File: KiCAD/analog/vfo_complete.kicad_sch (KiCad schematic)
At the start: 114 parts, among them J1 Filter Out, J10 Filter Out, J2 Filter Out, J3 Conn_01x02_Pin, J5 Conn_01x02_Pin, Q2 40673, Q3 2N3904, Q8 2N3904, U10 LM7171xIN, U11 LM7171xIN, U12 LM7171xIN, U13 LM7812_TO220, U14 LM317L_TO92, U21 LT1054, U22 LM7805_TO220, U5 Si5351A_Breakout, U9 MCP4921

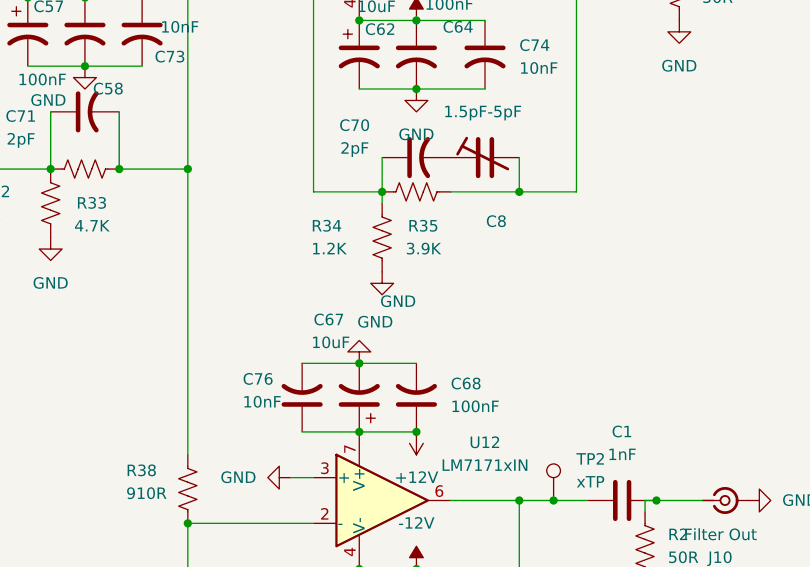
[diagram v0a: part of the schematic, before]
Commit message: KiCad revB: BFC2808 trimmer footprint for C8, verification checklist entry
- New custom footprint: xmitter:Trimmer_Vishay_BFC2808_D5mm_P5.08mm
  (radial THT, 5.08 mm pitch, 1.3 mm drill, Ø 2.4 mm pads, Ø 5.5 mm
  silk housing outline). Targets the top-adjustment 20508 variant of
  the 1.5-5 pF BFC2 808 series.
- Assigned that footprint to C8 (phase-trim cap across R35 in U11
  non-inv feedback). Datasheet property now points at the local PDF.
- Renamed source PDF: bfc2808-5mm.pdf → vishay-trimmer-cap.pdf (from
  a separate git-mv earlier in the session; references updated in
  three places to match).
- pcb_fab_checklist.md: new Section 1 sub-entry for the BFC2808
  footprint flagging (a) the 5.08 mm pitch assumption, (b) required
  1:1 paper-check against the physical part, (c) ordering-variant
  gotcha (20508 vs 23508 have different pitches).
- analog.kicad_pro: KiCad-driven used_designators expansion (RV1,
  #PWR14 added — cosmetic project metadata).

Co-Authored-By: Claude Opus 4.7 <noreply@anthropic.com>
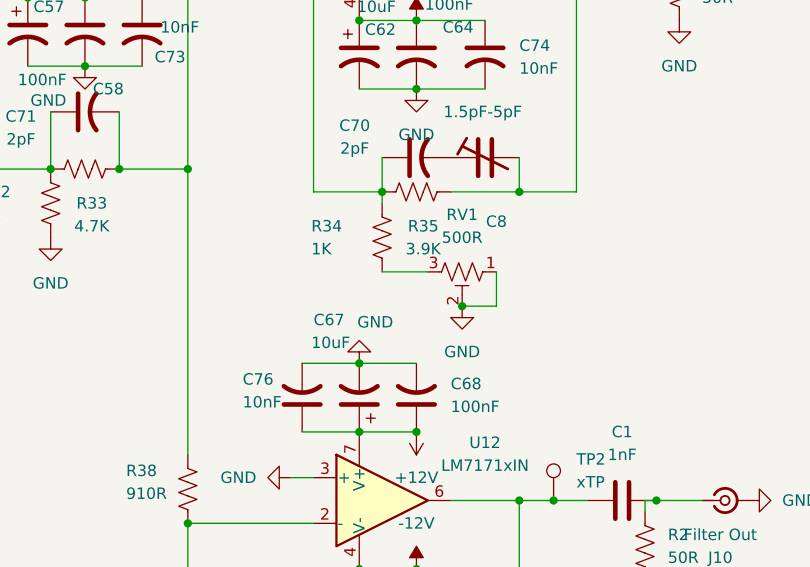
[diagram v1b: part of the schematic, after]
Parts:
- added RV1: 500R, symbol Device:R_Potentiometer_Trim_US
- C8: footprint (none) -> xmitter:Trimmer_Vishay_BFC2808_D5mm_P5.08mm
- R34: value 1.2K -> 1K
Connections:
- net GND: now also RV1.1, RV1.2; no longer R34.2
- new net: R34.2, RV1.3
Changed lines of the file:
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@@
 	)
 	(junction
+		(at 205.74 118.11)
+		(diameter 0)
+		(color 0 0 0 0)
+	)
+	(junction
 		(at 200.66 132.08)
 		(diameter 0)
@@
 	(wire
 		(pts
+			(xy 209.55 118.11) (xy 205.74 118.11)
+		)
+		(stroke
+			(width 0)
+			(type default)
+		)
+	)
+	(wire
+		(pts
 			(xy 147.32 35.56) (xy 149.86 35.56)
 		)
@@
 	(wire
 		(pts
+			(xy 209.55 114.3) (xy 209.55 118.11)
+		)
+		(stroke
+			(width 0)
+			(type default)
+		)
+	)
+	(wire
+		(pts
 			(xy 68.58 184.15) (xy 73.66 184.15)
 		)
@@
 	(wire
 		(pts
+			(xy 196.85 114.3) (xy 201.93 114.3)
+		)
+		(stroke
+			(width 0)
+			(type default)
+		)
+	)
+	(wire
+		(pts
 			(xy 54.61 177.8) (xy 73.66 177.8)
 		)
@@
 	(symbol
 		(lib_id "power:GND")
+		(at 205.74 118.11 0)
+		(unit 1)
+		(body_style 1)
+		(exclude_from_sim no)
+		(in_bom yes)
+		(on_board yes)
+		(in_pos_files yes)
+		(dnp no)
+		(fields_autoplaced yes)
+		(property "Reference" "#PWR014"
+			(at 205.74 124.46 0)
+			(hide yes)
+			(show_name no)
+			(do_not_autoplace no)
+			(effects
+				(font
+					(size 1.27 1.27)
+				)
+			)
+		)
+		(property "Value" "GND"
+			(at 205.74 123.19 0)
+			(show_name no)
+			(do_not_autoplace no)
+			(effects
+				(font
+					(size 1.27 1.27)
+				)
+			)
+		)
+		(property "Footprint" ""
+			(at 205.74 118.11 0)
+			(hide yes)
+			(show_name no)
+			(do_not_autoplace no)
+			(effects
+				(font
+					(size 1.27 1.27)
+				)
+			)
+		)
+		(property "Datasheet" ""
+			(at 205.74 118.11 0)
+			(hide yes)
+			(show_name no)
+			(do_not_autoplace no)
+			(effects
+				(font
+					(size 1.27 1.27)
+				)
+			)
+		)
+		(property "Description" "Power symbol creates a global label with name \"GND\" , ground"
+			(at 205.74 118.11 0)
+			(hide yes)
+			(show_name no)
+			(do_not_autoplace no)
+			(effects
+				(font
+					(size 1.27 1.27)
+				)
+			)
+		)
+		(pin "1"
+		)
+		(instances
+			(project "analog"
+				(path "/d3de40b8-856b-4fbd-829c-f45ffcd55742/94bbc356-fa50-4d6f-b6f0-2ea7eca96dd3"
+					(reference "#PWR014")
+					(unit 1)
+				)
+			)
+		)
+	)
+	(symbol
+		(lib_id "power:GND")
 		(at 43.18 82.55 0)
 		(unit 1)
@@
 			)
 		)
-		(property "Footprint" ""
+		(property "Footprint" "xmitter:Trimmer_Vishay_BFC2808_D5mm_P5.08mm"
 			(at 208.28 101.6 0)
 			(hide yes)
@@
 			)
 		)
-		(property "Datasheet" ""
+		(property "Datasheet" "Documentation/Components/vishay-trimmer-cap.pdf"
 			(at 208.28 101.6 0)
 			(hide yes)
@@
 	)
 	(symbol
+		(lib_id "Device:R_Potentiometer_Trim_US")
+		(at 205.74 114.3 270)
+		(unit 1)
+		(body_style 1)
+		(exclude_from_sim no)
+		(in_bom yes)
+		(on_board yes)
+		(in_pos_files yes)
+		(dnp no)
+		(fields_autoplaced yes)
+		(property "Reference" "RV1"
+			(at 205.74 107.95 90)
+			(show_name no)
+			(do_not_autoplace no)
+			(effects
+				(font
+					(size 1.27 1.27)
+				)
+			)
+		)
+		(property "Value" "500R"
+			(at 205.74 110.49 90)
+			(show_name no)
+			(do_not_autoplace no)
+			(effects
+				(font
+					(size 1.27 1.27)
+				)
+			)
+		)
+		(property "Footprint" ""
+			(at 205.74 114.3 0)
+			(hide yes)
+			(show_name no)
+			(do_not_autoplace no)
+			(effects
+				(font
+					(size 1.27 1.27)
+				)
+			)
+		)
+		(property "Datasheet" ""
+			(at 205.74 114.3 0)
+			(hide yes)
+			(show_name no)
+			(do_not_autoplace no)
+			(effects
+				(font
+					(size 1.27 1.27)
+				)
+			)
+		)
+		(property "Description" "Trim-potentiometer, US symbol"
+			(at 205.74 114.3 0)
+			(hide yes)
+			(show_name no)
+			(do_not_autoplace no)
+			(effects
+				(font
+					(size 1.27 1.27)
+				)
+			)
+		)
+		(property "Sim.Device" "R"
+			(at 205.74 114.3 0)
+			(hide yes)
+			(show_name no)
+			(do_not_autoplace no)
+			(effects
+				(font
+					(size 1.27 1.27)
+				)
+			)
+		)
+		(property "Sim.Type" "POT"
+			(at 205.74 114.3 0)
+			(hide yes)
+			(show_name no)
+			(do_not_autoplace no)
+			(effects
+				(font
+					(size 1.27 1.27)
+				)
+			)
+		)
+		(property "Sim.Pins" "1=r0 2=wiper 3=r1"
+			(at 205.74 114.3 0)
+			(hide yes)
+			(show_name no)
+			(do_not_autoplace no)
+			(effects
+				(font
+					(size 1.27 1.27)
+				)
+			)
+		)
+		(pin "1"
+		)
+		(pin "2"
+		)
+		(pin "3"
+		)
+		(instances
+			(project "analog"
+				(path "/d3de40b8-856b-4fbd-829c-f45ffcd55742/94bbc356-fa50-4d6f-b6f0-2ea7eca96dd3"
+					(reference "RV1")
+					(unit 1)
+				)
+			)
+		)
+	)
+	(symbol
 		(lib_id "power:GND")
 		(at 200.66 154.94 0)
@@
 	(symbol
 		(lib_id "power:GND")
-		(at 196.85 114.3 0)
-		(unit 1)
-		(body_style 1)
-		(exclude_from_sim no)
-		(in_bom yes)
-		(on_board yes)
-		(in_pos_files yes)
-		(dnp no)
-		(property "Reference" "#PWR0144"
-			(at 196.85 120.65 0)
-			(hide yes)
-			(show_name no)
-			(do_not_autoplace no)
-			(effects
-				(font
-					(size 1.27 1.27)
-				)
-			)
-		)
-		(property "Value" "GND"
-			(at 198.628 117.602 0)
-			(show_name no)
-			(do_not_autoplace no)
-			(effects
-				(font
-					(size 1.27 1.27)
-				)
-			)
-		)
-		(property "Footprint" ""
-			(at 196.85 114.3 0)
-			(hide yes)
-			(show_name no)
-			(do_not_autoplace no)
-			(effects
-				(font
-					(size 1.27 1.27)
-				)
-			)
-		)
-		(property "Datasheet" ""
-			(at 196.85 114.3 0)
-			(hide yes)
-			(show_name no)
-			(do_not_autoplace no)
-			(effects
-				(font
-					(size 1.27 1.27)
-				)
-			)
-		)
-		(property "Description" "Power symbol creates a global label with name \"GND\" , ground"
-			(at 196.85 114.3 0)
-			(hide yes)
-			(show_name no)
-			(do_not_autoplace no)
-			(effects
-				(font
-					(size 1.27 1.27)
-				)
-			)
-		)
-		(pin "1"
-		)
-		(instances
-			(project "analog"
-				(path "/d3de40b8-856b-4fbd-829c-f45ffcd55742/94bbc356-fa50-4d6f-b6f0-2ea7eca96dd3"
-					(reference "#PWR0144")
-					(unit 1)
-				)
-			)
-		)
-	)
-	(symbol
-		(lib_id "power:GND")
 		(at 120.65 81.28 0)
 		(unit 1)
@@
 			)
 		)
-		(property "Value" "1.2K"
+		(property "Value" "1K"
 			(at 188.976 111.76 0)
 			(show_name no)

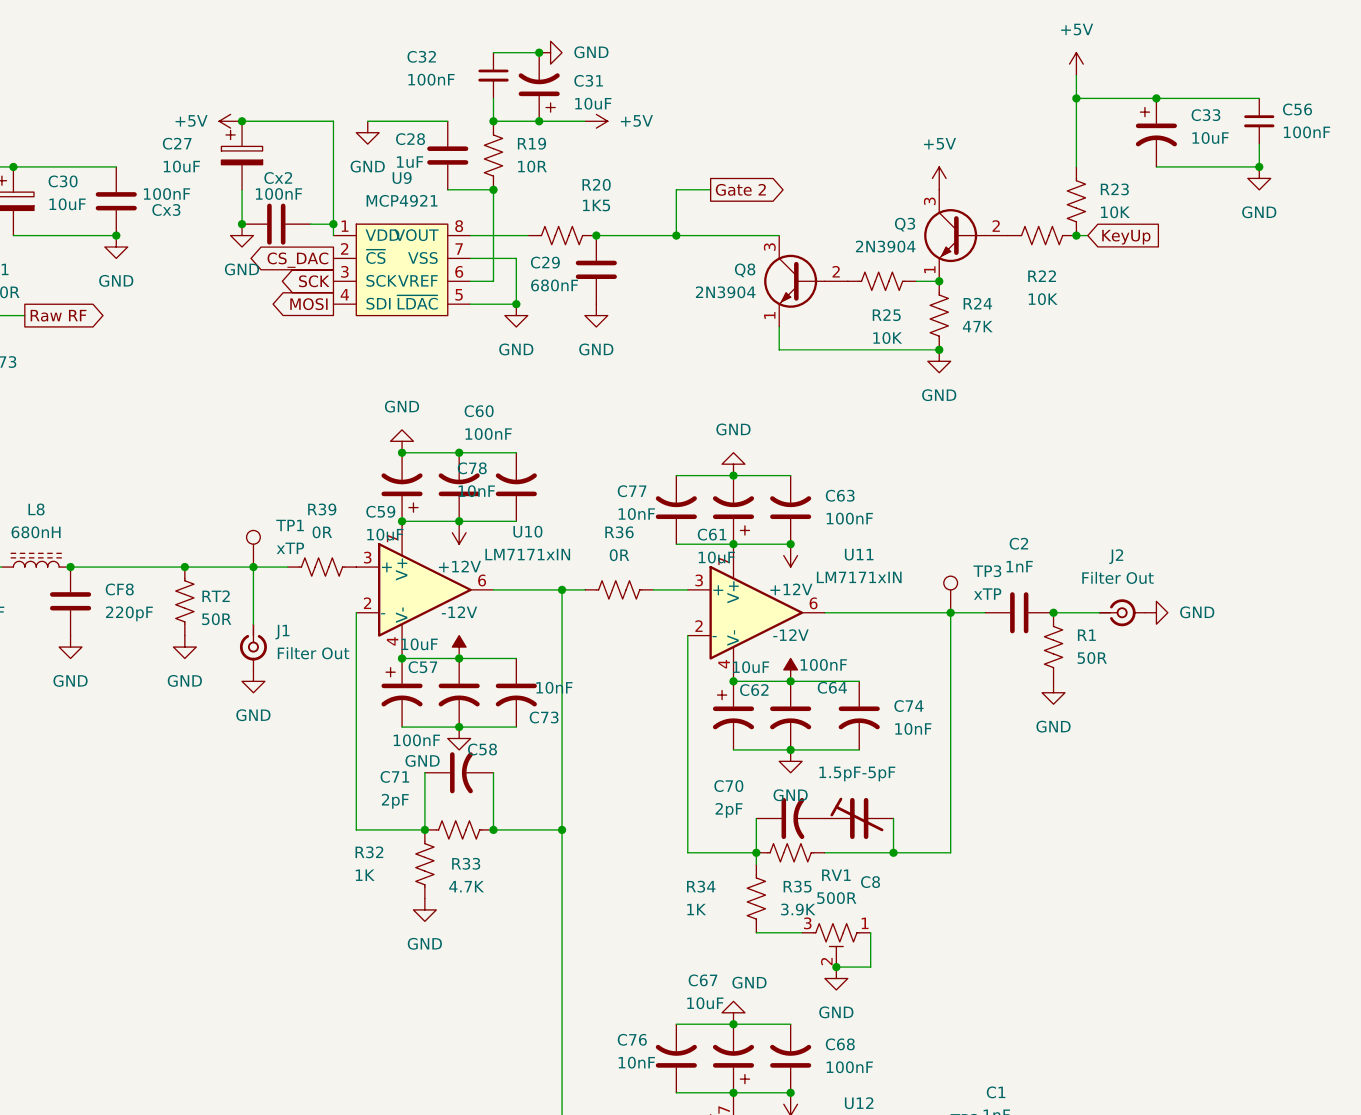
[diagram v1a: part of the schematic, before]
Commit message: revB frozen state: MCP4922 swap + LDAC decouple + sheet rename + protoshield work
Captures the in-flight state of revB at the point where the project pivoted
to a full-SS output stage on a new branch (SS_Rev_C, cut from this commit).
revB is retained as a fallback if the SS PA plan on revC proves inadequate.

Included changes:
- Analog: MCP4921 (single DAC) replaced with MCP4922 (dual DAC). Channel
  assignment: DAC_A -> PA_OUTPUT_LEVEL (new global label, awaiting PA
  board), DAC_B -> Gate 2 (DGFET envelope keyer). Channels swapped from
  initial-design intent for layout convenience.
- Analog: DAC_LDAC_N decoupled from PCF8575 P5 (that global label renamed
  to PCF_P5_SPARE). Intent: route LDAC to Metro A4 for zero-latency
  simultaneous-DAC-update capability. Physical route to A4 NOT yet added
  -- DAC_LDAC_N label on dac.kicad_sch is dangling and will fail ERC.
- Analog: KiCad-driven used_designators bookkeeping (analog.kicad_pro).
- Sheet rename: KiCAD/analog/untitled.kicad_sch -> dac.kicad_sch. Root
  schematic Sheetfile reference updated.
- Protoshield: 537 lines of additions to protoshield.kicad_sch (user
  work). Not reviewed in this commit -- carried forward as-is.
- .gitignore: added tools/_*.py exclusion (local review-helper scripts).

**revB is NOT fab-ready in this state.** See memory
project_revB_pre_fab_check.md (outside repo) for the punch list. If the
SS PA plan ever reverses and someone revives revB, ALL open items must
be closed and a full pass through Documentation/pcb_fab_checklist.md
must be completed before any gerber submit.

Co-Authored-By: Claude Opus 4.7 <noreply@anthropic.com>
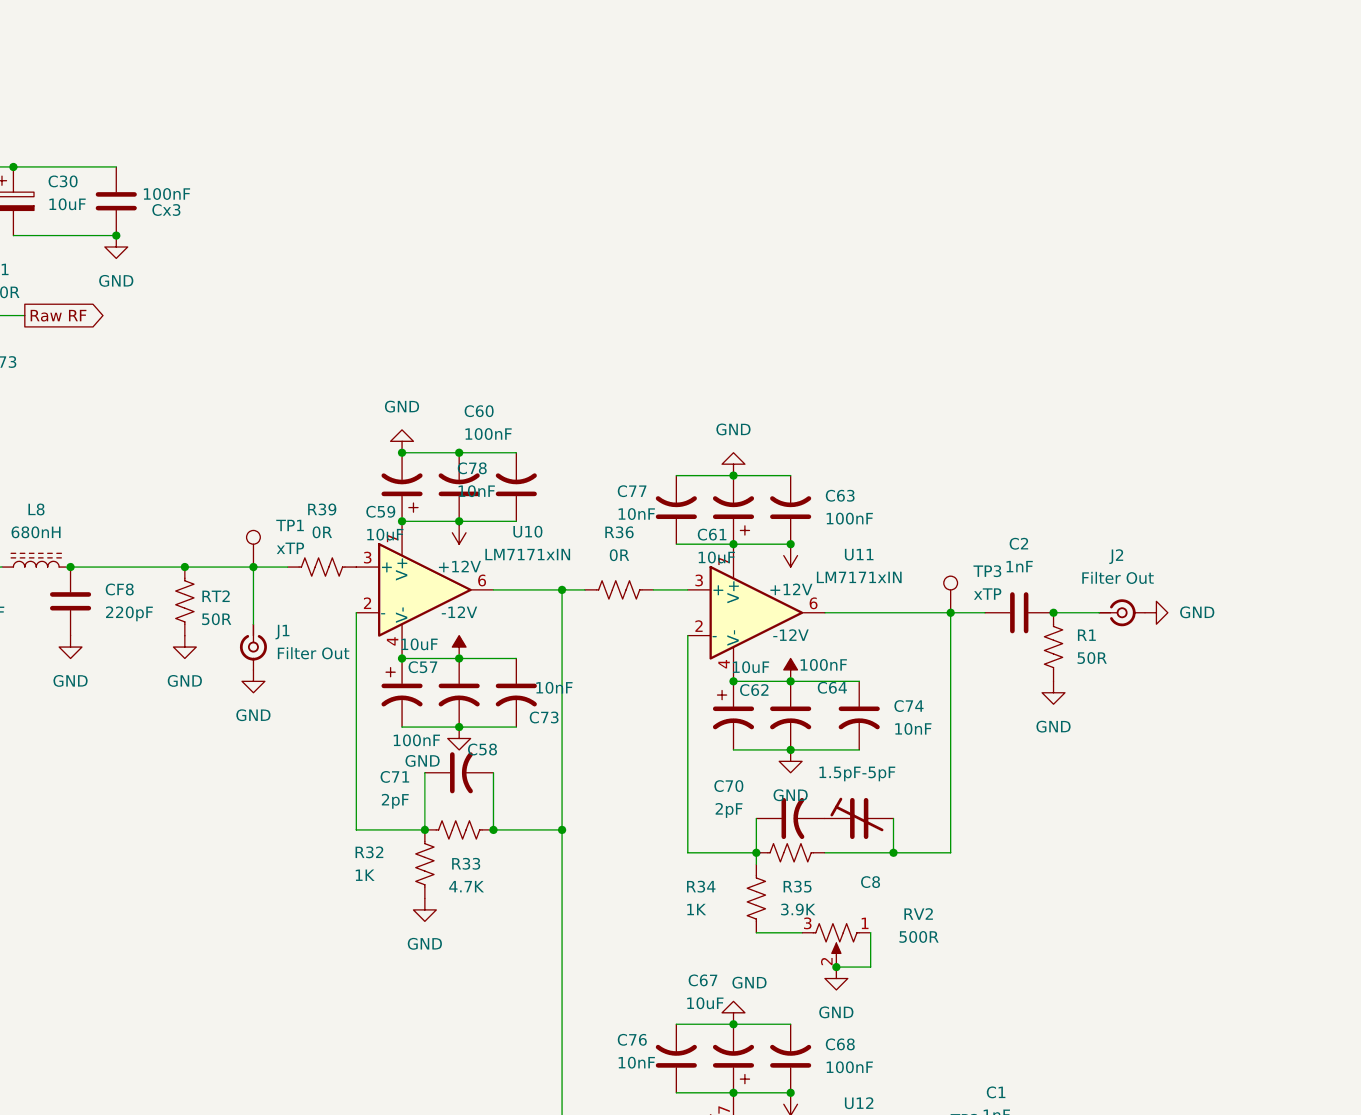
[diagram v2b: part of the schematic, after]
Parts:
- removed C27: 10uF, Capacitor_THT:C_Rect_L7.2mm_W4.5mm_P5.00mm, symbol Device:C_Polarized
- removed C28: 1uF, Capacitor_THT:C_Rect_L7.2mm_W4.5mm_P5.00mm, symbol Device:C
- removed C29: 680nF, Capacitor_THT:C_Rect_L13.0mm_W6.0mm_P10.00mm_FKS3_FKP3_MKS4, symbol Device:C
- removed C31, C33: 10uF, Capacitor_THT:CP_Radial_D5.0mm_P2.00mm, symbol Device:C_Polarized_US
- removed C32, C56: 100nF, Capacitor_THT:C_Disc_D5.0mm_W2.5mm_P5.00mm, symbol Device:C_Small
- removed Cx2: 100nF, Capacitor_THT:C_Disc_D5.0mm_W2.5mm_P5.00mm, symbol Device:C
- removed Q3, Q8: 2N3904, Package_TO_SOT_THT:TO-92_Inline_Wide, symbol Transistor_BJT:2N3904
- removed R19: 10R, Resistor_THT:R_Axial_DIN0207_L6.3mm_D2.5mm_P10.16mm_Horizontal, symbol Device:R_US
- removed R20: 1K5, Resistor_THT:R_Axial_DIN0207_L6.3mm_D2.5mm_P10.16mm_Horizontal, symbol Device:R_US
- removed R22, R23, R25: 10K, Resistor_THT:R_Axial_DIN0207_L6.3mm_D2.5mm_P10.16mm_Horizontal, symbol Device:R_US
- removed R24: 47K, Resistor_THT:R_Axial_DIN0207_L6.3mm_D2.5mm_P10.16mm_Horizontal, symbol Device:R_US
- removed RV1: 500R, symbol Device:R_Potentiometer_Trim_US
- removed U9: MCP4921, Package_DIP:DIP-8_W7.62mm, symbol xmitter:MCP4921
- added RV2: 500R, Potentiometer_THT:Potentiometer_Bourns_3296W_Vertical, symbol Device:R_Potentiometer_US
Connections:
- net GND: now also RV2.1, RV2.2
- net at R34.2: now also RV2.3
